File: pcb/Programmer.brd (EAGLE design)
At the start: 160 x 100 mm, 5 parts, among them J1 MINI-USB-JACK, U1 FT232HQ, U2 SN74AVCH4T245RSVR, X1 SIT8021

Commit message: Progress creating programmer board
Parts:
- added R5: 10k, EagleLibrary:0402
- added U3, U4, U5, U6, U7: SN74LV1T125DCKR, EagleLibrary:SN74LV1T12XDCKR
- added U8, U9: SN74LV1T126DCKR, EagleLibrary:SN74LV1T12XDCKR
- U2: value SN74AVCH4T245RSVR -> SN74LV1T125DCKR; device EagleLibrary:SN74AVCH4T245RSVR -> EagleLibrary:SN74LV1T12XDCKR
- moved U2 7.18 mm to (2.54, -2.54)
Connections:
- removed net N$10: U2.16
- removed net N$12: U2.5
- removed net N$5: U2.8
- removed net N$6: U2.9
- removed net N$7: U2.13
- removed net N$8: U2.12
- new net FLASH_MODE: U6.1, U7.1, U8.1, U9.1
- new net FTDI_CDONE: U5.4
- new net FTDI_CRESET_: U4.2
- new net FTDI_CS_: U3.2
- new net FTDI_SCLK: U2.2
- new net FTDI_SI: U7.4, U9.4
- new net FTDI_SO: U6.2, U8.2
- new net ICE_CDONE: R5.2, U5.2
- new net ICE_CRESET_: U4.4
- new net ICE_CS_: U3.4
- new net ICE_SCLK: U2.4
- new net ICE_SI: U6.4, U9.2
- new net ICE_SO: U7.2, U8.4
- net 1V8: now also R5.1, U2.5, U3.5, U4.5, U6.5, U8.5; no longer U2.2
- net 3V3: now also U5.5, U7.5, U9.5; no longer U2.3, U2.4
- net GND: now also U2.3, U3.1, U3.3, U4.1, U4.3, U5.1, U5.3, U6.3, U7.3, U8.3, U9.3; no longer U2.10, U2.11
- net N$1: now also U1.13; no longer U2.6
- net N$2: now also U1.14; no longer U2.7
- net N$3: now also U1.15; no longer U2.15
- net N$4: now also U1.16; no longer U2.14

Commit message: Progress creating programmer board
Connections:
- net ICE_CDONE renamed ICE_PRG_CDONE
- net ICE_CRESET_ renamed ICE_PRG_CRESET_
- net ICE_CS_ renamed ICE_PRG_CS_
- net ICE_SCLK renamed ICE_PRG_CLK
- net ICE_SI renamed ICE_PRG_DI
- net ICE_SO renamed ICE_PRG_DO
- removed net FLASH_MODE: U6.1, U7.1, U8.1, U9.1
- removed net FTDI_CDONE: U5.4
- removed net FTDI_CRESET_: U4.2
- removed net FTDI_CS_: U3.2
- removed net FTDI_SCLK: U2.2
- removed net FTDI_SI: U7.4, U9.4
- removed net FTDI_SO: U6.2, U8.2
- removed net N$1: U1.13
- removed net N$2: U1.14
- removed net N$3: U1.15
- removed net N$4: U1.16
- new net CLK12MHZ: X1.2
- new net FTDI_FLASH_MODE: U1.18, U6.1, U7.1, U8.1, U9.1
- new net FTDI_PRG_CDONE: U1.19, U5.4
- new net FTDI_PRG_CLK: U1.13, U2.2
- new net FTDI_PRG_CRESET_: U1.20, U4.2
- new net FTDI_PRG_CS_: U1.17, U3.2
- new net FTDI_PRG_DI: U1.15, U7.4, U9.4
- new net FTDI_PRG_DO: U1.14, U6.2, U8.2
- net 3V3: now also X1.3
- net GND: now also X1.1, X1.4
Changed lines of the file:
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@@
 <contactref element="U7" pad="5"/>
 <contactref element="U9" pad="5"/>
+<contactref element="X1" pad="3"/>
+<wire x1="35.1275" y1="35.56" x2="35.765" y2="37.6" width="0" layer="19" extent="1-1"/>
 <wire x1="3.5023" y1="-13.32" x2="35.1275" y2="35.56" width="0" layer="19" extent="1-1"/>
 <wire x1="3.5023" y1="-23.48" x2="3.5023" y2="-13.32" width="0" layer="19" extent="1-1"/>
@@
 <contactref element="U8" pad="3"/>
 <contactref element="U9" pad="3"/>
+<contactref element="X1" pad="4"/>
+<contactref element="X1" pad="1"/>
+<wire x1="35.355" y1="38.6" x2="35.765" y2="38.6" width="0" layer="19" extent="1-1"/>
+<wire x1="35.9925" y1="35.56" x2="35.765" y2="38.6" width="0" layer="19" extent="1-1"/>
 <wire x1="1.5777" y1="-1.89" x2="35.9925" y2="35.56" width="0" layer="19" extent="1-1"/>
 <wire x1="1.5777" y1="-3.19" x2="1.5777" y2="-1.89" width="0" layer="19" extent="1-1"/>
@@
 <wire x1="3.5023" y1="-1.89" x2="3.5023" y2="-5.7" width="0" layer="19" extent="1-1"/>
 </signal>
-<signal name="FTDI_SCLK">
+<signal name="FTDI_PRG_CLK">
 <contactref element="U2" pad="2"/>
+<contactref element="U1" pad="13"/>
+<wire x1="1.5777" y1="-2.54" x2="22.65" y2="21.5244" width="0" layer="19" extent="1-1"/>
 </signal>
-<signal name="ICE_SCLK">
+<signal name="ICE_PRG_CLK">
 <contactref element="U2" pad="4"/>
 </signal>
-<signal name="FTDI_CS_">
+<signal name="FTDI_PRG_CS_">
 <contactref element="U3" pad="2"/>
+<contactref element="U1" pad="17"/>
+<wire x1="1.5777" y1="-6.35" x2="24.65" y2="21.5244" width="0" layer="19" extent="1-1"/>
 </signal>
-<signal name="ICE_CS_">
+<signal name="ICE_PRG_CS_">
 <contactref element="U3" pad="4"/>
 </signal>
-<signal name="FTDI_CRESET_">
+<signal name="FTDI_PRG_CRESET_">
 <contactref element="U4" pad="2"/>
+<contactref element="U1" pad="20"/>
+<wire x1="1.5777" y1="-10.16" x2="26.15" y2="21.5244" width="0" layer="19" extent="1-1"/>
 </signal>
-<signal name="ICE_CRESET_">
+<signal name="ICE_PRG_CRESET_">
 <contactref element="U4" pad="4"/>
 </signal>
-<signal name="ICE_CDONE">
+<signal name="ICE_PRG_CDONE">
 <contactref element="U5" pad="2"/>
 <contactref element="R5" pad="2"/>
 <wire x1="1.5777" y1="-13.97" x2="1.7025" y2="-16.51" width="0" layer="19" extent="1-1"/>
 </signal>
-<signal name="FTDI_CDONE">
+<signal name="FTDI_PRG_CDONE">
 <contactref element="U5" pad="4"/>
+<contactref element="U1" pad="19"/>
+<wire x1="3.5023" y1="-14.62" x2="25.65" y2="21.5244" width="0" layer="19" extent="1-1"/>
 </signal>
-<signal name="FTDI_SO">
+<signal name="FTDI_PRG_DO">
 <contactref element="U6" pad="2"/>
 <contactref element="U8" pad="2"/>
-<wire x1="1.5777" y1="-20.32" x2="1.5777" y2="-27.94" width="0" layer="19" extent="1-1"/>
+<contactref element="U1" pad="14"/>
+<wire x1="1.5777" y1="-20.32" x2="23.15" y2="21.5244" width="0" layer="19" extent="1-1"/>
+<wire x1="1.5777" y1="-27.94" x2="1.5777" y2="-20.32" width="0" layer="19" extent="1-1"/>
 </signal>
-<signal name="FLASH_MODE">
+<signal name="ICE_PRG_DI">
+<contactref element="U6" pad="4"/>
+<contactref element="U9" pad="2"/>
+<wire x1="3.5023" y1="-20.97" x2="1.5777" y2="-31.75" width="0" layer="19" extent="1-1"/>
+</signal>
+<signal name="ICE_PRG_DO">
+<contactref element="U7" pad="2"/>
+<contactref element="U8" pad="4"/>
+<wire x1="1.5777" y1="-24.13" x2="3.5023" y2="-28.59" width="0" layer="19" extent="1-1"/>
+</signal>
+<signal name="FTDI_PRG_DI">
+<contactref element="U7" pad="4"/>
+<contactref element="U9" pad="4"/>
+<contactref element="U1" pad="15"/>
+<wire x1="3.5023" y1="-24.78" x2="23.65" y2="21.5244" width="0" layer="19" extent="1-1"/>
+<wire x1="3.5023" y1="-32.4" x2="3.5023" y2="-24.78" width="0" layer="19" extent="1-1"/>
+</signal>
+<signal name="FTDI_FLASH_MODE">
+<contactref element="U1" pad="18"/>
 <contactref element="U6" pad="1"/>
 <contactref element="U7" pad="1"/>
 <contactref element="U9" pad="1"/>
 <contactref element="U8" pad="1"/>
-<wire x1="1.5777" y1="-27.29" x2="1.5777" y2="-31.1" width="0" layer="19" extent="1-1"/>
-<wire x1="1.5777" y1="-23.48" x2="1.5777" y2="-27.29" width="0" layer="19" extent="1-1"/>
-<wire x1="1.5777" y1="-19.67" x2="1.5777" y2="-23.48" width="0" layer="19" extent="1-1"/>
+<wire x1="1.5777" y1="-19.67" x2="25.15" y2="21.5244" width="0" layer="19" extent="1-1"/>
+<wire x1="1.5777" y1="-23.48" x2="1.5777" y2="-19.67" width="0" layer="19" extent="1-1"/>
+<wire x1="1.5777" y1="-27.29" x2="1.5777" y2="-23.48" width="0" layer="19" extent="1-1"/>
+<wire x1="1.5777" y1="-31.1" x2="1.5777" y2="-27.29" width="0" layer="19" extent="1-1"/>
 </signal>
-<signal name="ICE_SI">
-<contactref element="U6" pad="4"/>
-<contactref element="U9" pad="2"/>
-<wire x1="3.5023" y1="-20.97" x2="1.5777" y2="-31.75" width="0" layer="19" extent="1-1"/>
-</signal>
-<signal name="ICE_SO">
-<contactref element="U7" pad="2"/>
-<contactref element="U8" pad="4"/>
-<wire x1="1.5777" y1="-24.13" x2="3.5023" y2="-28.59" width="0" layer="19" extent="1-1"/>
-</signal>
-<signal name="FTDI_SI">
-<contactref element="U7" pad="4"/>
-<contactref element="U9" pad="4"/>
-<wire x1="3.5023" y1="-24.78" x2="3.5023" y2="-32.4" width="0" layer="19" extent="1-1"/>
-</signal>
-<signal name="N$1">
-<contactref element="U1" pad="13"/>
-</signal>
-<signal name="N$2">
-<contactref element="U1" pad="14"/>
-</signal>
-<signal name="N$3">
-<contactref element="U1" pad="15"/>
-</signal>
-<signal name="N$4">
-<contactref element="U1" pad="16"/>
+<signal name="CLK12MHZ">
+<contactref element="X1" pad="2"/>
 </signal>
 </signals>

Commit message: Finished with programmer schematic
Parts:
- added C1, C10, C11, C13, C14, C16, C17, C18, C19, C20, C21, C22, C23, C3, C5, C7, C9: 100n, EagleLibrary:0402
- added C12, C4, C6, C8: 10u, EagleLibrary:1206
- added C15, C2: 10n, EagleLibrary:0402
- added FB1, FB2, FB3: FERRITE-BEAD1206, EagleLibrary:1206
- added H1: WURTH-61201021621, EagleLibrary:WURTH-61201021621
- added R1: 12k, EagleLibrary:0402
- added R2: 10k, EagleLibrary:0402
- added U10: TPD4S012DRYR, EagleLibrary:TPD4S012DRYR
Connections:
- new net 5V: C12.1, C3.1, FB1.2, H1.6, U1.40
- new net N$1: C2.1, R2.2, U1.34
- new net N$13: H1.9
- new net N$3: C11.1, U1.37
- new net N$4: R1.1, U1.5
- new net N$5: C1.1, U1.38
- new net USB_D+: J1.D+, U1.7, U10.1
- new net USB_D-: J1.D-, U1.6, U10.2
- new net VBUS: C15.1, FB1.1, J1.VCC, U10.6
- new net VPHY: C4.1, C5.1, FB2.2, U1.3
- new net VPLL: C6.1, C7.1, FB3.2, U1.8
- net 1V8: now also C16.1, C17.1, C18.1, C19.1, C20.1, H1.7
- net 3V3: now also C10.1, C13.1, C14.1, C21.1, C22.1, C23.1, C8.1, C9.1, FB2.1, FB3.1, R2.1, U1.12, U1.24, U1.39, U1.46
- net CLK12MHZ: now also U1.1
- net GND: now also C1.2, C10.2, C11.2, C12.2, C13.2, C14.2, C15.2, C16.2, C17.2, C18.2, C19.2, C2.2, C20.2, C21.2, C22.2, C23.2, C3.2, C4.2, C5.2, C6.2, C7.2, C8.2, C9.2, H1.8, J1.GND, J1.GND2, J1.GND3, J1.GND4, J1.GND5, R1.2, U1.10, U1.11, U1.22, U1.23, U1.35, U1.36, U1.4, U1.41, U1.42, U1.47, U1.48, U1.49, U1.9, U10.4
- net ICE_PRG_CDONE: now also H1.5
- net ICE_PRG_CLK: now also H1.2
- net ICE_PRG_CRESET_: now also H1.10
- net ICE_PRG_CS_: now also H1.3
- net ICE_PRG_DI: now also H1.1
- net ICE_PRG_DO: now also H1.4

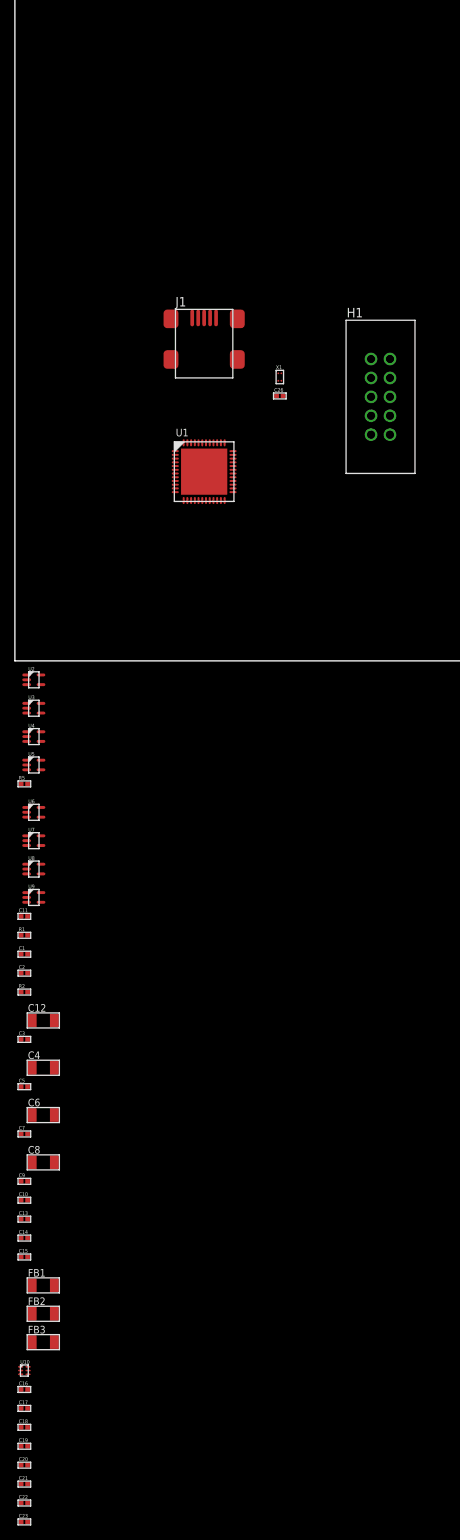
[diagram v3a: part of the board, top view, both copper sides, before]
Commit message: Programmer board progress. Trying to decide whether we can reliably support UART...
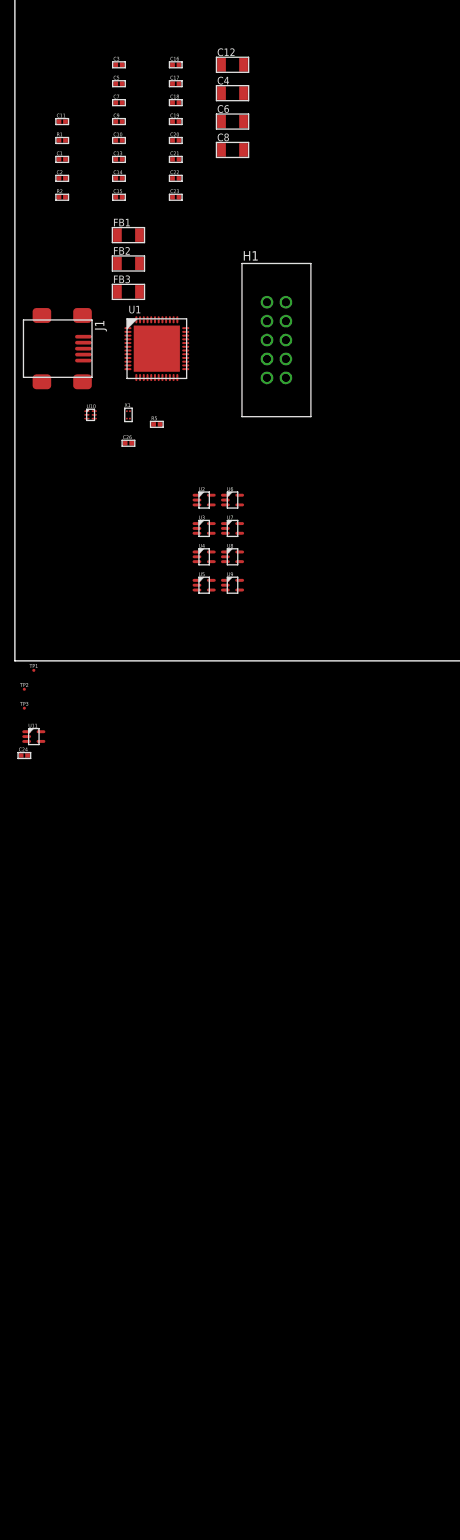
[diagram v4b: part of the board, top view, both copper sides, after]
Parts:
- added C24: 100n, EagleLibrary:0402
- added TP1, TP2, TP3: TEST-POINT, EagleLibrary:TEST-POINT
- added U11: SN74LV1T125DCKR, EagleLibrary:SN74LV1T12XDCKR
- U8, U9: value SN74LV1T126DCKR -> SN74LV1T125DCKR
- moved C16 179.0 mm to (21.6, 80.0)
- moved C17 179.0 mm to (21.6, 77.5)
- moved C18 179.0 mm to (21.6, 74.9)
- moved C19 179.0 mm to (21.6, 72.4)
- moved C20 179.0 mm to (21.6, 69.8)
- moved C21 179.0 mm to (21.6, 67.3)
- moved C22 179.0 mm to (21.6, 64.8)
- moved C23 179.0 mm to (21.6, 62.2)
- moved C10 142.8 mm to (14.0, 69.8)
- moved C13 142.8 mm to (14.0, 67.3)
- moved C14 142.8 mm to (14.0, 64.8)
- moved C15 142.8 mm to (14.0, 62.2)
- moved C9 142.8 mm to (14.0, 72.4)
- moved FB1 141.4 mm to (15.2, 57.1)
- moved FB2 141.4 mm to (15.2, 53.3)
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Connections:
- removed net FTDI_FLASH_MODE: U1.18, U6.1, U7.1, U8.1, U9.1
- new net FTDI_FLASH_EN_: U1.25, U8.1, U9.1
- new net FTDI_SRAM_EN_: U1.21, U6.1, U7.1
- new net FTDI_UART_EN_: U1.26, U11.1
- net 3V3: now also C24.1, TP3.X, U11.5
- net 5V: now also TP2.X
- net CLK12MHZ: now also TP1.X
- net FTDI_PRG_DO: now also U11.4
- net GND: now also C24.2, U11.3
- net ICE_PRG_DO: now also U11.2

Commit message: Commit before switching to 74LV1T126
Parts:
- removed C24: 100n, EagleLibrary:0402
- removed U11: SN74LV1T125DCKR, EagleLibrary:SN74LV1T12XDCKR
- added H2: HEADER-1X3, EagleLibrary:HEADER-1X3
- U8, U9: value SN74LV1T125DCKR -> SN74LV1T126DCKR
- moved C22 55.0 mm to (25.4, 9.93), flipped to the bottom, turned to 270 degrees
- moved C23 52.9 mm to (29.2, 9.93), flipped to the bottom, turned to 270 degrees
- moved C21 50.3 mm to (29.2, 17.6), flipped to the bottom, turned to 270 degrees
- moved C18 48.8 mm to (15.4, 26.5), flipped to the bottom
- moved C16 48.1 mm to (17.8, 32.1), turned to 180 degrees
- moved C19 46.0 mm to (18.3, 26.5), flipped to the bottom
- moved C17 45.5 mm to (17.8, 32.1), flipped to the bottom
- moved C6 37.5 mm to (11.3, 39.4), flipped to the bottom
- moved C20 36.8 mm to (13.3, 34.0), flipped to the bottom
- moved C4 35.4 mm to (11.3, 45.7), flipped to the bottom
- moved C7 34.1 mm to (12.6, 40.9), flipped to the bottom
- moved C5 33.3 mm to (12.6, 44.2), flipped to the bottom
- moved C3 32.9 mm to (20.1, 47.7)
- moved C12 31.8 mm to (21.4, 49.2)
- moved C10 31.6 mm to (14.0, 38.3), turned to 270 degrees
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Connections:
- net FTDI_PRG_CRESET_ renamed FTDI_PRG_CRST_
- net ICE_PRG_CRESET_ renamed ICE_PRG_CRST_
- removed net FTDI_FLASH_EN_: U1.25, U8.1, U9.1
- removed net FTDI_SRAM_EN_: U1.21, U6.1, U7.1
- removed net FTDI_UART_EN_: U1.26, U11.1
- new net FTDI_FLASH_MODE: U1.21, U6.1, U7.1, U8.1, U9.1
- net 3V3: no longer C24.1, U11.5
- net FTDI_PRG_DI: now also H2.2
- net FTDI_PRG_DO: now also H2.1; no longer U11.4
- net GND: now also H2.3; no longer C24.2, U11.3
- net ICE_PRG_DO: no longer U11.2
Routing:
- net GND: track 0.00 -> 59.2 mm, vias 0 -> 33
- net 3V3: track 0.00 -> 18.4 mm, vias 0 -> 11
- net ICE_PRG_DI: track 0.00 -> 16.8 mm, vias 0 -> 1
- net ICE_PRG_CLK: track 0.00 -> 13.2 mm
- net 1V8: track 0.00 -> 9.44 mm, vias 0 -> 4
- net USB_D-: track 0.00 -> 8.03 mm, vias 0 -> 1
- net USB_D+: track 0.00 -> 8.01 mm, vias 0 -> 1
- net VBUS: track 0.00 -> 6.39 mm, vias 0 -> 1
- net FTDI_PRG_CLK: track 0.00 -> 6.24 mm
- net VPLL: track 0.00 -> 5.90 mm, vias 0 -> 1
- net FTDI_PRG_DO: track 0.00 -> 5.55 mm, vias 0 -> 1
- net VPHY: track 0.00 -> 5.35 mm, vias 0 -> 1
- net 5V: track 0.00 -> 4.57 mm, vias 0 -> 2
- net N$4: track 0.00 -> 2.52 mm, vias 0 -> 1
- net ICE_PRG_CDONE: track 0.00 -> 2.16 mm, vias 0 -> 1
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- added copper zone on layer 1, net GND1
- added copper zone on layer 16, net GND1
- added copper zone on layer 2, net GND1
- added copper zone on layer 15, net VDD

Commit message: Finished laying out programmer board
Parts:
- moved TP3 57.3 mm to (20.5, 47.7), flipped to the bottom
- moved TP2 54.7 mm to (19.7, 47.7), flipped to the bottom
- moved TP1 47.7 mm to (13.8, 45.0)
- moved H2 46.7 mm to (12.7, 30.6), turned to 90 degrees
- moved C23 28.3 mm to (16.7, 35.4), flipped to the top
- moved U9 27.0 mm to (18.3, 34.8), turned to 90 degrees
- moved C22 25.8 mm to (20.9, 35.4), flipped to the top
- moved C18 25.1 mm to (37.0, 39.5), turned to 270 degrees
- moved U5 24.8 mm to (22.4, 34.8), turned to 90 degrees
- moved R5 24.1 mm to (24.0, 34.0), flipped to the top, turned to 270 degrees
- moved C21 23.7 mm to (13.6, 35.4), flipped to the top
- moved U3 23.3 mm to (35.4, 38.9), flipped to the bottom, turned to 90 degrees
- moved C19 22.2 mm to (28.4, 46.3), turned to 270 degrees
- moved U7 22.1 mm to (15.2, 34.8), turned to 90 degrees
- moved U4 20.9 mm to (26.9, 45.7), flipped to the bottom, turned to 90 degrees
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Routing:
- net FTDI_FLASH_MODE: track 0.00 -> 41.1 mm, vias 0 -> 5
- net FTDI_PRG_DO: track 5.55 -> 41.9 mm, vias 1 -> 4
- net GND: track 59.2 -> 87.6 mm, vias 33 -> 36
- net FTDI_PRG_CS_: track 0.00 -> 27.2 mm, vias 0 -> 1
- net ICE_PRG_DO: track 0.00 -> 24.2 mm, vias 0 -> 1
- net FTDI_PRG_DI: track 0.00 -> 22.2 mm, vias 0 -> 2
- net FTDI_PRG_CLK: track 6.24 -> 25.7 mm, vias 0 -> 3
- net ICE_PRG_CDONE: track 2.16 -> 18.7 mm
- net FTDI_PRG_CRST_: track 0.00 -> 15.2 mm, vias 0 -> 1
- net ICE_PRG_CLK: track 13.2 -> 2.43 mm
- net FTDI_PRG_CDONE: track 0.00 -> 5.95 mm
- net ICE_PRG_CRST_: track 0.00 -> 4.18 mm
- net ICE_PRG_DI: track 16.8 -> 20.2 mm
- net ICE_PRG_CS_: track 0.00 -> 2.20 mm
- net 5V: track 4.57 -> 5.46 mm
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- added copper zone on layer 15, net 1V8
- added copper zone on layer 15, net 3V3
- added copper zone on layer 15, net 5V
- added copper zone on layer 1, net GND
- added copper zone on layer 16, net GND
- added copper zone on layer 2, net GND
- removed copper zone on layer 1, net GND1
- removed copper zone on layer 16, net GND1
- removed copper zone on layer 2, net GND1
- removed copper zone on layer 15, net VDD
